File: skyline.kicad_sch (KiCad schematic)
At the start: 134 parts, among them J2 USB_C_Receptacle_USB2.0_16P, J5 Conn_01x05, J7 Battery, Q3 AO3401A, Q5 2N7002, Q6 AO3401A, SW4 RST, SW7 PWR, SW8 RotaryEncoder_Switch, U10 TP4056, U4 PRTR5V0U2X, U5 nRF52840_holyiot_18010, U7 XC6206PxxxMR

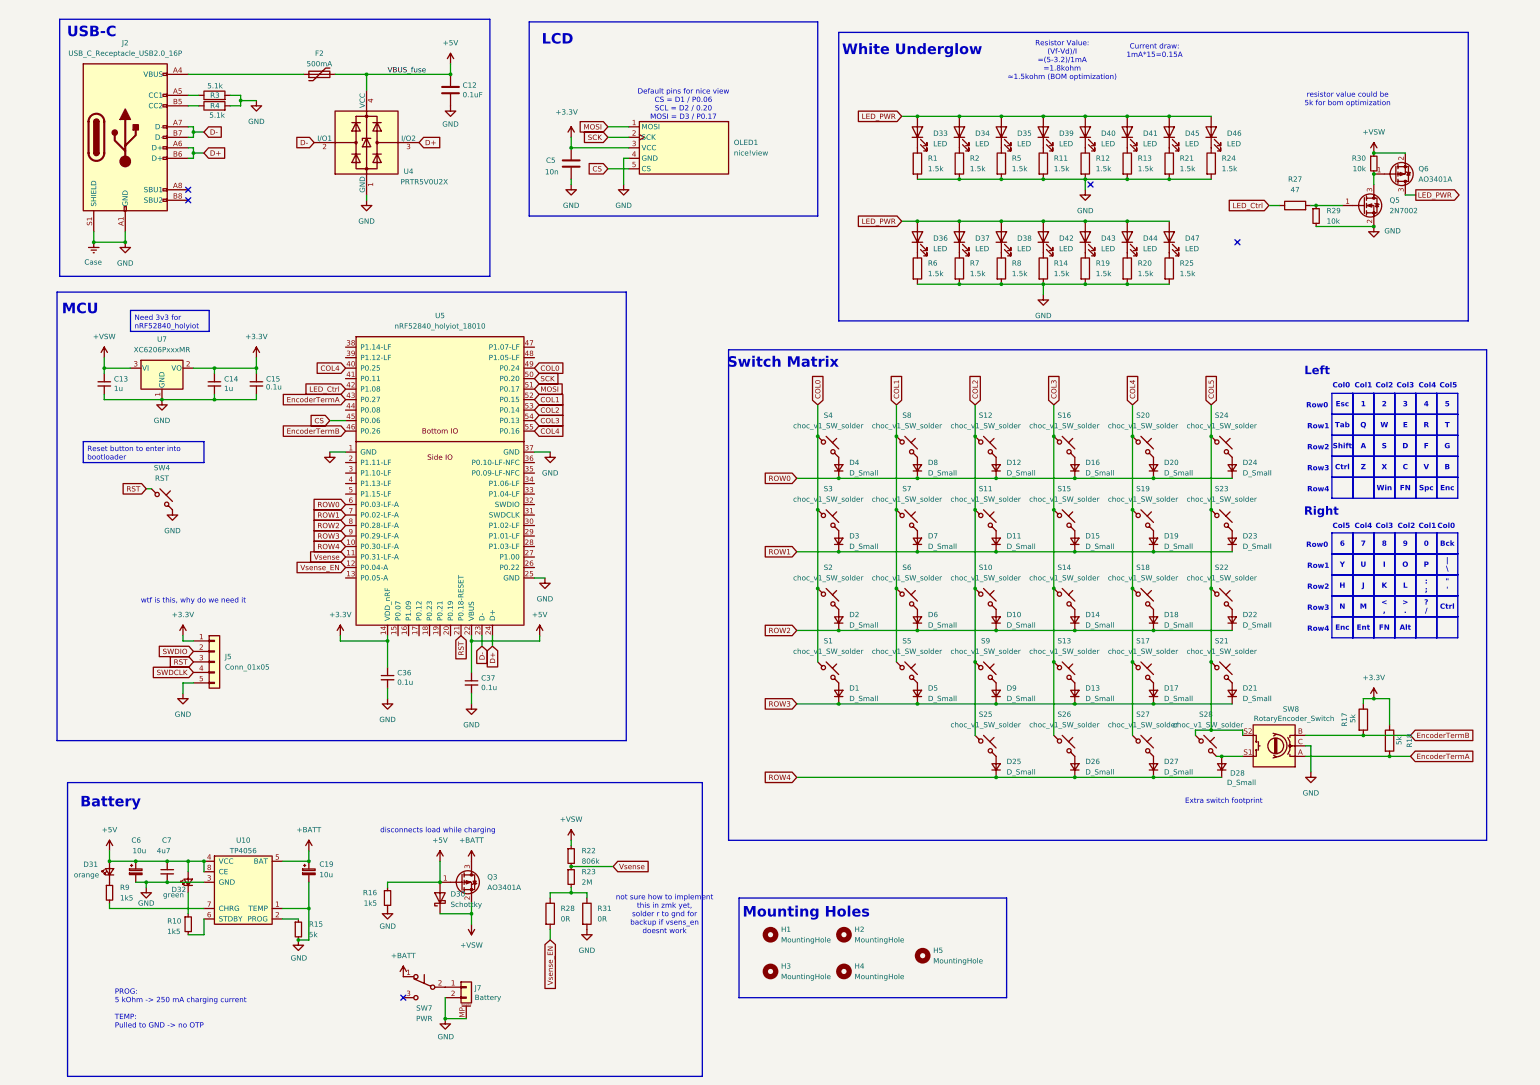
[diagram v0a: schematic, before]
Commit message: Added rev. led footprints, jumpers for niceview
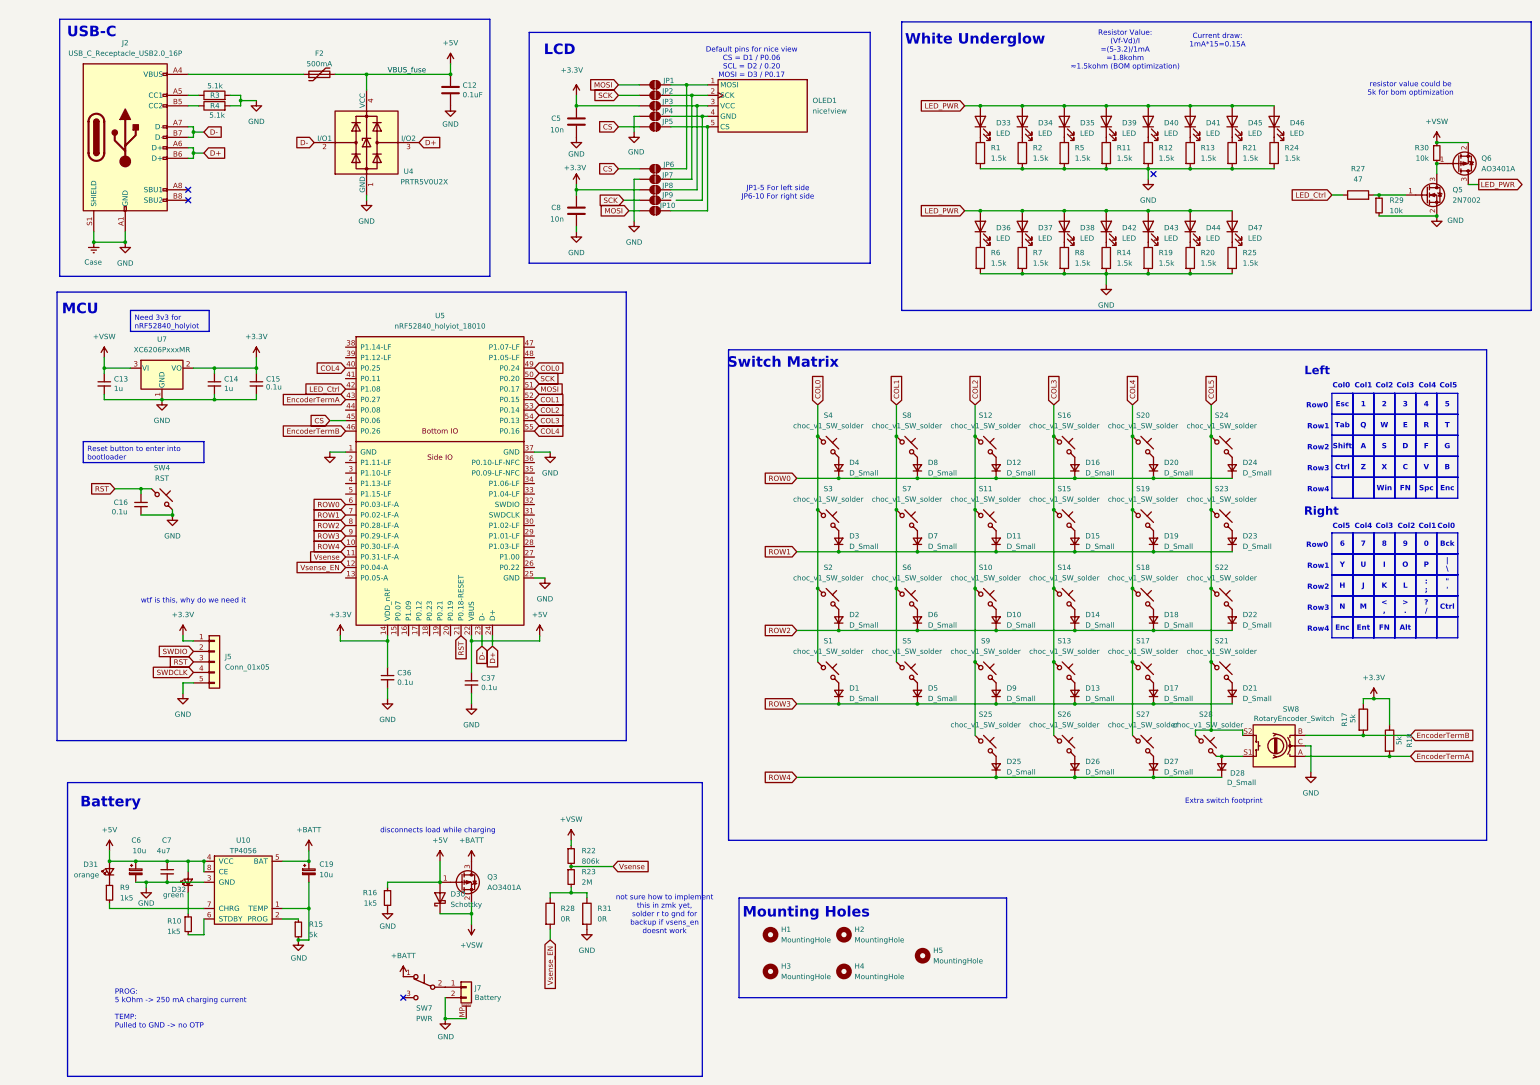
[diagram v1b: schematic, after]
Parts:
- added C16: 0.1u, Capacitor_SMD:C_0402_1005Metric, symbol Device:C_Small
- added C8: 10n, symbol Device:C
- added JP1, JP10, JP2, JP3, JP4, JP5, JP6, JP7, JP8, JP9: SolderJumper_2_Open, reversible_skyline:Jumper_solder, symbol Jumper:SolderJumper_2_Open
- D1, D10, D11, D12, D13, D14, D15, D16, D17, D18, D19, D2, D20, D21, D22, D23, D24, D25, D26, D27, D28, D3, D4, D5, D6, D7, D8, D9: footprint Diode_SMD:D_0805_2012Metric_Pad1.15x1.40mm_HandSolder -> reversible_skyline:reversible_D_0805_2012Metric_Pad1.15x1.40mm_HandSolder
- D33, D34, D35, D36, D37, D38, D39, D40, D41, D42, D43, D44, D45, D46, D47: footprint LED_THT:LED_D5.0mm -> reversible_skyline:reversible_D_0805_2012Metric_Pad1.15x1.40mm_HandSolder
- J5: footprint (none) -> Connector_PinHeader_2.54mm:PinHeader_1x05_P2.54mm_Vertical
- S1, S10, S11, S12, S13, S14, S15, S16, S17, S18, S19, S2, S20, S21, S22, S23, S24, S25, S26, S27, S28, S3, S4, S5, S6, S7, S8, S9: footprint PCM_marbastlib-choc:SW_choc_v1_1u -> PCM_marbastlib-xp-choc:SW_choc_Reversible_1u
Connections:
- net +3.3V: now also C8.1, JP3.1 (A), JP8.1 (A); no longer OLED1.3 (VCC)
- net CS: now also JP5.1 (A), JP6.1 (A); no longer OLED1.5 (CS)
- net Case: now also C16.2, C8.2, JP4.1 (A), JP7.1 (A); no longer OLED1.4 (GND)
- net MOSI: now also JP1.1 (A), JP10.1 (A); no longer OLED1.1 (MOSI)
- net RST: now also C16.1
- net SCK: now also JP2.1 (A), JP9.1 (A); no longer OLED1.2 (SCK)
- new net: JP10.2 (B), JP5.2 (B), OLED1.5 (CS)
- new net: JP4.2 (B), OLED1.4 (GND)
- new net: JP3.2 (B), JP8.2 (B), OLED1.3 (VCC)
- new net: JP1.2 (B), JP6.2 (B), OLED1.1 (MOSI)
- new net: JP2.2 (B), JP7.2 (B), OLED1.2 (SCK)
- no-connect marks 5 -> 4
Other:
- note added: "JP1-5 For left side JP6-10 For right side"
- moved on the sheet: C5, D33, D34, D35, D36, D37, D38, D39, D40, D41, D42, D43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

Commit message: finished routing, need to fix it up now
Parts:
- removed C12: 0.1uF, Capacitor_SMD:C_0402_1005Metric, symbol Device:C
- removed C13, C14: 1u, Capacitor_SMD:C_0402_1005Metric, symbol Device:C_Small
- removed C15, C16, C36, C37: 0.1u, Capacitor_SMD:C_0402_1005Metric, symbol Device:C_Small
- removed C19, C6: 10u, symbol Device:C_Polarized_Small
- removed C5, C8: 10n, symbol Device:C
- removed C7: 4u7, Capacitor_SMD:C_0402_1005Metric, symbol Device:C_Small
- removed D1, D10, D11, D12, D13, D14, D15, D16, D17, D18, D19, D2, D20, D21, D22, D23, D24, D25, D26, D27, D28, D3, D4, D5, D6, D7, D8, D9: D_Small, reversible_skyline:reversible_D_0805_2012Metric_Pad1.15x1.40mm_HandSolder, symbol Device:D_Small
- removed D30: Schottky, symbol Device:D_Schottky
- removed D31: orange, LED_SMD:LED_0402_1005Metric_Pad0.77x0.64mm_HandSolder, symbol Device:LED_Small
- removed D32: green, LED_SMD:LED_0402_1005Metric_Pad0.77x0.64mm_HandSolder, symbol Device:LED_Small
- removed D33, D34, D35, D36, D37, D38, D39, D40, D41, D42, D43, D44, D45, D46, D47: LED, reversible_skyline:reversible_D_0805_2012Metric_Pad1.15x1.40mm_HandSolder, symbol Device:LED
- removed F2: 500mA, Fuse:Fuse_1206_3216Metric, symbol Device:Polyfuse
- removed H1, H2, H3, H4, H5: MountingHole, MountingHole:MountingHole_2.2mm_M2_DIN965_Pad, symbol Mechanical:MountingHole
- removed J2: USB_C_Receptacle_USB2.0_16P, symbol Connector:USB_C_Receptacle_USB2.0_16P
- removed J5: Conn_01x05, Connector_PinHeader_2.54mm:PinHeader_1x05_P2.54mm_Vertical, symbol Connector_Generic:Conn_01x05
- removed J7: Battery, PCM_marbastlib-various:Molex_Pico-EZmate_78171-0002_1x02-1MP_P1.20mm_Vertical, symbol Connector_Generic_MountingPin:Conn_01x02_MountingPin
- removed JP1, JP10, JP2, JP3, JP4, JP5, JP6, JP7, JP8, JP9: SolderJumper_2_Open, reversible_skyline:Jumper_solder, symbol Jumper:SolderJumper_2_Open
- removed OLED1: nice!view, nice_view:nice_view, symbol nice_view:nice!view
- removed Q3, Q6: AO3401A, Package_TO_SOT_SMD:SOT-23, symbol Transistor_FET:AO3401A
- removed Q5: 2N7002, Package_TO_SOT_SMD:SOT-23, symbol Transistor_FET:2N7002
- removed R1, R11, R12, R13, R14, R19, R2, R20, R21, R24, R25, R5, R6, R7, R8: 1.5k, LED_SMD:LED_0805_2012Metric_Pad1.15x1.40mm_HandSolder, symbol Device:R
- removed R10, R16, R9: 1k5, Resistor_SMD:R_0402_1005Metric, symbol Device:R_Small
- removed R15: 5k, Resistor_SMD:R_0402_1005Metric, symbol Device:R_Small
- removed R17, R18: 5k, Resistor_SMD:R_0603_1608Metric_Pad0.98x0.95mm_HandSolder, symbol Device:R
- removed R22: 806k, Resistor_SMD:R_0402_1005Metric, symbol Device:R_Small
- removed R23: 2M, Resistor_SMD:R_0402_1005Metric, symbol Device:R_Small
- removed R27: 47, Resistor_SMD:R_0805_2012Metric_Pad1.20x1.40mm_HandSolder, symbol Device:R
- removed R28, R31: 0R, symbol Device:R
- removed R29, R30: 10k, Resistor_SMD:R_0402_1005Metric, symbol Device:R_Small
- removed R3, R4: 5.1k, Resistor_SMD:R_0402_1005Metric_Pad0.72x0.64mm_HandSolder, symbol Device:R
- removed S1, S10, S11, S12, S13, S14, S15, S16, S17, S18, S19, S2, S20, S21, S22, S23, S24, S25, S26, S27, S28, S3, S4, S5, S6, S7, S8, S9: choc_v1_SW_solder, PCM_marbastlib-xp-choc:SW_choc_Reversible_1u, symbol PCM_marbastlib-choc:choc_v1_SW_solder
- removed SW4: RST, PCM_marbastlib-various:SW_SPST_SKQG_WithStem, symbol Switch:SW_Push_45deg
- removed SW7: PWR, PCM_marbastlib-various:SW_MSK12C02-HB, symbol Switch:SW_Push_SPDT
- removed SW8: RotaryEncoder_Switch, PCM_marbastlib-various:ROT_Alps_EC11E-Switch, symbol Device:RotaryEncoder_Switch
- removed U10: TP4056, Package_SO:SOP-8-1EP_4.57x4.57mm_P1.27mm_EP4.57x4.45mm, symbol PCM_marbastlib-various:TP4056
- removed U4: PRTR5V0U2X, Package_TO_SOT_SMD:SOT-143, symbol Power_Protection:PRTR5V0U2X
- removed U5: nRF52840_holyiot_18010, PCM_marbastlib-various:nRF52840_holyiot_18010, symbol PCM_marbastlib-various:nRF52840_holyiot_18010
- removed U7: XC6206PxxxMR, Package_TO_SOT_SMD:SOT-23, symbol Regulator_Linear:XC6206PxxxMR
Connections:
- no-connect marks 4 -> 0
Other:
- added sheet left (left.kicad_sch)
- added sheet right (right.kicad_sch)
- note removed: "" '"
- note removed: "0"
- note removed: "1"
- note removed: "2"
- note removed: "3"
- note removed: "4"
- note removed: "5"
- note removed: "6"
- note removed: "7"
- note removed: "8"
- note removed: "9"
- note removed: ": ;"
- note removed: "< ,"
- note removed: "> ."
- note removed: "? /"
- note removed: "A"
- note removed: "Alt"
- note removed: "B"
- note removed: "Battery"
- note removed: "Bck"
- note removed: "C"
- note removed: "Col0"
- note removed: "Col1"
- note removed: "Col2"
- note removed: "Col3"
- note removed: "Col4"
- note removed: "Col5"
- note removed: "Ctrl"
- note removed: "Current draw: 1mA*15=0.15A"
- note removed: "D"
- note removed: "Default pins for nice view CS = D1 / P0.06 SCL = D2 / 0.20 MOSI = D3 / P0.17"
- note removed: "E"
- note removed: "Enc"
- note removed: "Ent"
- note removed: "Esc"
- note removed: "Extra switch footprint"
- note removed: "F"
- note removed: "FN"
- note removed: "G"
- note removed: "H"
- note removed: "I"
- note removed: "J"
- note removed: "JP1-5 For left side JP6-10 For right side"
- note removed: "K"
- note removed: "L"
- note removed: "LCD"
- note removed: "Left"
- note removed: "M"
- note removed: "MCU"
- note removed: "Mounting Holes"
- note removed: "N"
- note removed: "O"
- note removed: "P"
- note removed: "PROG: 5 kOhm -> 250 mA charging current TEMP: Pulled to GND -> no OTP"
- note removed: "Q"
- note removed: "R"
- note removed: "Resistor Value: (Vf-Vd)/I =(5-3.2)/1mA =1.8kohm ≈1.5kohm (BOM optimization)"
- note removed: "Right"
- note removed: "Row0"
- note removed: "Row1"
- note removed: "Row2"
- note removed: "Row3"
- note removed: "Row4"
- note removed: "S"
- note removed: "Shift"
- note removed: "Spc"
- note removed: "Switch Matrix"
- note removed: "T"
- note removed: "Tab"
- note removed: "U"
- note removed: "USB-C"
- note removed: "V"
- note removed: "W"
- note removed: "White Underglow"
- note removed: "Win"
- note removed: "X"
- note removed: "Y"
- note removed: "Z"
- note removed: "disconnects load while charging"
- note removed: "not sure how to implement this in zmk yet, solder r to gnd for backup if vsens_en doesnt work"
- note removed: "resistor value could be 5k for bom optimization"
- note removed: "wtf is this, why do we need it"
- note removed: "| \"
